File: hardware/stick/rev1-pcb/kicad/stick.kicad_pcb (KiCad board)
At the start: 4 copper layers, 60 x 30 mm, 13 parts, among them J1 USB4135-GF-A, J2 GDEY0154D67, SW1 BTN_L, SW2 BTN_R, U1 IP4292CZ12, U2 TPS2553, U3 AP2112K-3.3, U4 nRF52840, U5 ATECC608B, Y1 32MHz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

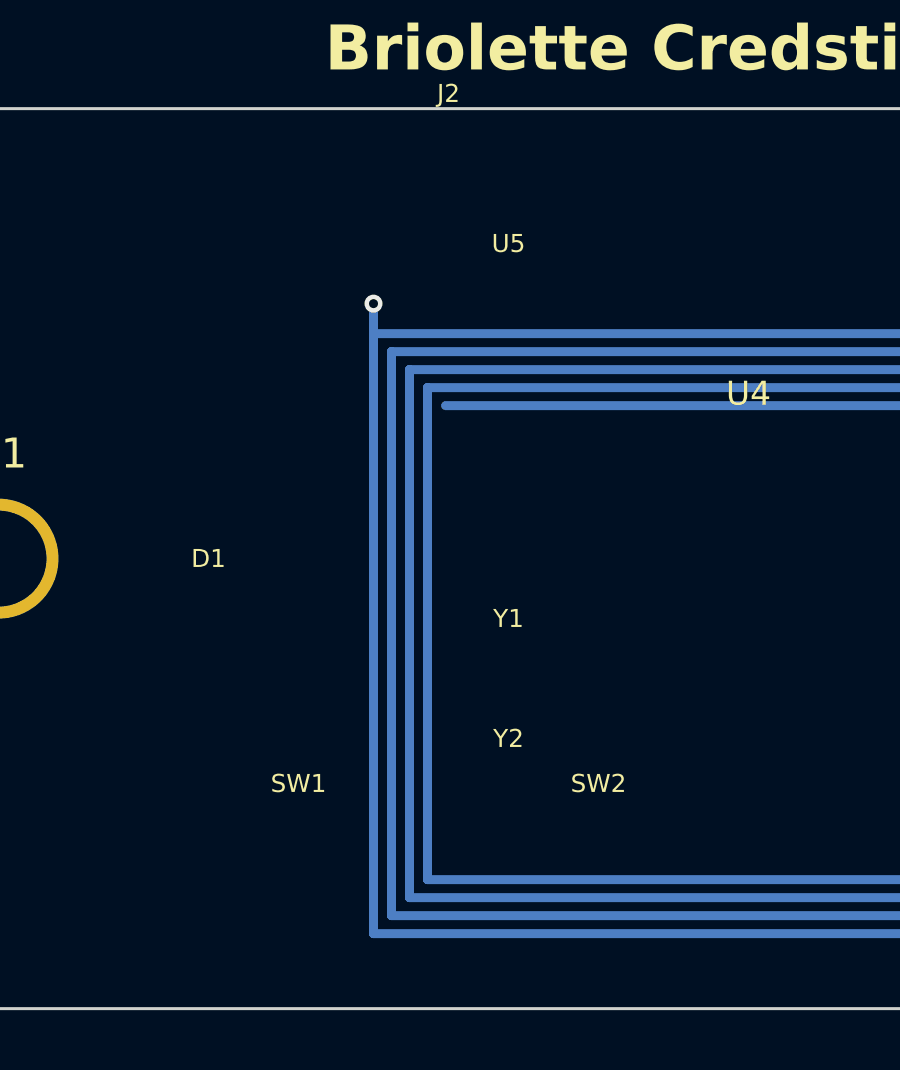
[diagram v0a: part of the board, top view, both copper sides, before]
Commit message: Fix DOA-causing issues in credstick and relay PCB designs
Critical fixes:
- HASL→ENIG copper finish on both PCBs (QFN pads need flat surface)
- Replace stale ATECC608B footprint with Nano-SIM connector on credstick PCB
- Fix NFC antenna spirals: closed rectangles→continuous spiral with crossover vias
- Fix TCA8418/SW3 component overlap at (-20,-15) on relay PCB
- Add missing inter-sheet pins (EPD_BUSY, BTN_L/R, LED, VSCAP_SENSE) to credstick top-level
- Fix button footprints (SW_SPST_PTS810→SW_SPST_3x3mm) to match schematic
- Replace stale I2C nets (SDA/SCL) with SIM interface nets
- Fix nRF52840 package description in both BOMs (aQFN-73 7x7→QFN-48 6x6)
- Remove ATECC608B reference from credstick BOM sourcing guide

https://claude.ai/code/session_01TM1rFxbipYtvAkh4Vt7My7
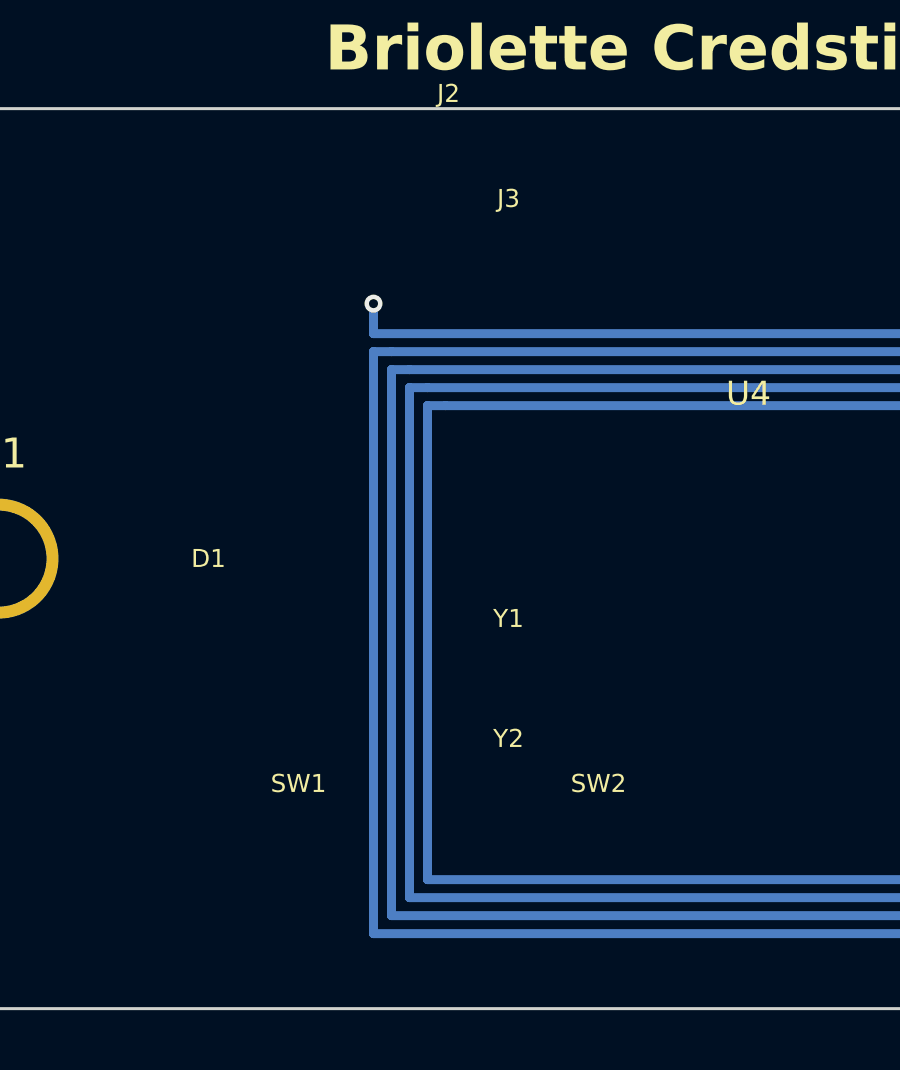
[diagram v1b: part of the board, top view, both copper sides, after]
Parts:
- removed U5: ATECC608B, stick-lib:UDFN-8-2x3mm
- added J3: Nano-SIM Push-Push, stick-lib:NanoSIM_Molex_78800, F.Cu at (-8.00, -8.00)
- SW1, SW2: footprint Button_Switch_SMD:SW_SPST_PTS810 -> stick-lib:SW_SPST_3x3mm
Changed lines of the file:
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@@
       (layer "B.Paste" (type "Bottom Solder Paste"))
       (layer "B.SilkS" (type "Bottom Silk Screen"))
-      (copper_finish "HASL with lead")
+      (copper_finish "ENIG")
       (dielectric_constraints no)
     )
@@
   (net 3 "VBUS")
   (net 4 "VSCAP")
-  (net 5 "SDA")
-  (net 6 "SCL")
+  (net 5 "SIM_IO")
+  (net 6 "SIM_CLK")
+  (net 29 "SIM_RST")
+  (net 30 "SIM_DET")
   (net 7 "SPI_SCK")
   (net 8 "SPI_MOSI")
@@
     )
   )
-  ;; --- ATECC608B: near MCU, I2C side ---
-  (footprint "stick-lib:UDFN-8-2x3mm"
+  ;; --- Nano-SIM connector: near MCU, ISO 7816 interface ---
+  (footprint "stick-lib:NanoSIM_Molex_78800"
     (layer "F.Cu")
     (at -8.0 -8.0 0)
-    (property "Reference" "U5"
-      (at 0 -2.5 0)
-      (layer "F.SilkS")
-      (effects (font (size 0.6 0.6) (thickness 0.1)))
-    )
-    (property "Value" "ATECC608B"
-      (at 0 2.5 0)
+    (property "Reference" "J3"
+      (at 0 -4.0 0)
+      (layer "F.SilkS")
+      (effects (font (size 0.6 0.6) (thickness 0.1)))
+    )
+    (property "Value" "Nano-SIM Push-Push"
+      (at 0 4.0 0)
       (layer "F.Fab")
       (effects (font (size 0.6 0.6) (thickness 0.1)))
@@
   )
   ;; --- Left button: below display, left side ---
-  (footprint "Button_Switch_SMD:SW_SPST_PTS810"
+  (footprint "stick-lib:SW_SPST_3x3mm"
     (layer "F.Cu")
     (at -15.0 10.0 0)
@@
   )
   ;; --- Right button: below display, right side ---
-  (footprint "Button_Switch_SMD:SW_SPST_PTS810"
+  (footprint "stick-lib:SW_SPST_3x3mm"
     (layer "F.Cu")
     (at -5.0 10.0 0)
@@
   ;; Centered at (0, 2) on the bottom layer
   ;; ============================================================
-  ;; Turn 1 (outermost): 25x20mm
-  (gr_line (start -12.5 -7.5) (end 12.5 -7.5)
-    (stroke (width 0.3) (type default)) (layer "B.Cu") (net 24))
-  (gr_line (start 12.5 -7.5) (end 12.5 12.5)
-    (stroke (width 0.3) (type default)) (layer "B.Cu") (net 24))
-  (gr_line (start 12.5 12.5) (end -12.5 12.5)
-    (stroke (width 0.3) (type default)) (layer "B.Cu") (net 24))
-  (gr_line (start -12.5 12.5) (end -12.5 -7.5)
-    (stroke (width 0.3) (type default)) (layer "B.Cu") (net 24))
-  ;; Turn 2: inset by 0.6mm (24.8x19.8 → ±11.9, ±6.9/±11.9)
-  (gr_line (start -11.9 -6.9) (end 11.9 -6.9)
-    (stroke (width 0.3) (type default)) (layer "B.Cu") (net 24))
-  (gr_line (start 11.9 -6.9) (end 11.9 11.9)
-    (stroke (width 0.3) (type default)) (layer "B.Cu") (net 24))
-  (gr_line (start 11.9 11.9) (end -11.9 11.9)
-    (stroke (width 0.3) (type default)) (layer "B.Cu") (net 24))
-  (gr_line (start -11.9 11.9) (end -11.9 -6.9)
-    (stroke (width 0.3) (type default)) (layer "B.Cu") (net 24))
-  ;; Turn 3: inset by another 0.6mm
-  (gr_line (start -11.3 -6.3) (end 11.3 -6.3)
-    (stroke (width 0.3) (type default)) (layer "B.Cu") (net 24))
-  (gr_line (start 11.3 -6.3) (end 11.3 11.3)
-    (stroke (width 0.3) (type default)) (layer "B.Cu") (net 24))
-  (gr_line (start 11.3 11.3) (end -11.3 11.3)
-    (stroke (width 0.3) (type default)) (layer "B.Cu") (net 24))
-  (gr_line (start -11.3 11.3) (end -11.3 -6.3)
-    (stroke (width 0.3) (type default)) (layer "B.Cu") (net 24))
-  ;; Turn 4: inset by another 0.6mm
-  (gr_line (start -10.7 -5.7) (end 10.7 -5.7)
-    (stroke (width 0.3) (type default)) (layer "B.Cu") (net 24))
-  (gr_line (start 10.7 -5.7) (end 10.7 10.7)
-    (stroke (width 0.3) (type default)) (layer "B.Cu") (net 24))
-  (gr_line (start 10.7 10.7) (end -10.7 10.7)
-    (stroke (width 0.3) (type default)) (layer "B.Cu") (net 24))
-  (gr_line (start -10.7 10.7) (end -10.7 -5.7)
-    (stroke (width 0.3) (type default)) (layer "B.Cu") (net 24))
-  ;; Turn 5 (innermost half-turn, connects to NFC2 via)
-  (gr_line (start -10.1 -5.1) (end 10.1 -5.1)
-    (stroke (width 0.3) (type default)) (layer "B.Cu") (net 25))
-  (gr_line (start 10.1 -5.1) (end 10.1 10.1)
-    (stroke (width 0.3) (type default)) (layer "B.Cu") (net 25))
-  ;; Spiral interconnects (short jumps between turns)
-  ;; Outer start → Turn 1 connects via trace to NFC1 pad via
-  (gr_line (start -12.5 -7.5) (end -12.5 -8.5)
-    (stroke (width 0.3) (type default)) (layer "B.Cu") (net 24))
-  ;; Inner end connects via to NFC2 pad
-  (gr_line (start 10.1 10.1) (end 10.1 11.0)
-    (stroke (width 0.3) (type default)) (layer "B.Cu") (net 25))
-  ;; NFC vias (connect bottom antenna to top-layer NFC pads)
+  ;; NFC Antenna: Continuous rectangular spiral, 4.5 turns
+  ;; Each turn is open at bottom-left corner and steps inward to next turn.
+  ;; Trace width: 0.3mm, spacing: 0.3mm, pitch: 0.6mm
+  ;; All turns on single net (NFC_ANT), inner end crosses to NFC2 via top layer.
+  ;; Start: via from F.Cu NFC1 pad down to B.Cu at (-12.5, -8.5)
   (via (at -12.5 -8.5) (size 0.6) (drill 0.3)
     (layers "F.Cu" "B.Cu") (net 24))
+  ;; Lead-in from via to Turn 1 start
+  (gr_line (start -12.5 -8.5) (end -12.5 -7.5)
+    (stroke (width 0.3) (type default)) (layer "B.Cu") (net 24))
+  ;; Turn 1 (outermost): 3 sides — top, right, bottom (open at left)
+  (gr_line (start -12.5 -7.5) (end 12.5 -7.5)
+    (stroke (width 0.3) (type default)) (layer "B.Cu") (net 24))
+  (gr_line (start 12.5 -7.5) (end 12.5 12.5)
+    (stroke (width 0.3) (type default)) (layer "B.Cu") (net 24))
+  (gr_line (start 12.5 12.5) (end -12.5 12.5)
+    (stroke (width 0.3) (type default)) (layer "B.Cu") (net 24))
+  ;; Left side stops short — step inward to Turn 2
+  (gr_line (start -12.5 12.5) (end -12.5 -6.9)
+    (stroke (width 0.3) (type default)) (layer "B.Cu") (net 24))
+  ;; Step inward (connects Turn 1 left to Turn 2 top-left)
+  (gr_line (start -12.5 -6.9) (end -11.9 -6.9)
+    (stroke (width 0.3) (type default)) (layer "B.Cu") (net 24))
+  ;; Turn 2: 3 sides — top, right, bottom (open at left)
+  (gr_line (start -11.9 -6.9) (end 11.9 -6.9)
+    (stroke (width 0.3) (type default)) (layer "B.Cu") (net 24))
+  (gr_line (start 11.9 -6.9) (end 11.9 11.9)
+    (stroke (width 0.3) (type default)) (layer "B.Cu") (net 24))
+  (gr_line (start 11.9 11.9) (end -11.9 11.9)
+    (stroke (width 0.3) (type default)) (layer "B.Cu") (net 24))
+  ;; Left side stops short — step inward to Turn 3
+  (gr_line (start -11.9 11.9) (end -11.9 -6.3)
+    (stroke (width 0.3) (type default)) (layer "B.Cu") (net 24))
+  (gr_line (start -11.9 -6.3) (end -11.3 -6.3)
+    (stroke (width 0.3) (type default)) (layer "B.Cu") (net 24))
+  ;; Turn 3: 3 sides — top, right, bottom (open at left)
+  (gr_line (start -11.3 -6.3) (end 11.3 -6.3)
+    (stroke (width 0.3) (type default)) (layer "B.Cu") (net 24))
+  (gr_line (start 11.3 -6.3) (end 11.3 11.3)
+    (stroke (width 0.3) (type default)) (layer "B.Cu") (net 24))
+  (gr_line (start 11.3 11.3) (end -11.3 11.3)
+    (stroke (width 0.3) (type default)) (layer "B.Cu") (net 24))
+  ;; Left side stops short — step inward to Turn 4
+  (gr_line (start -11.3 11.3) (end -11.3 -5.7)
+    (stroke (width 0.3) (type default)) (layer "B.Cu") (net 24))
+  (gr_line (start -11.3 -5.7) (end -10.7 -5.7)
+    (stroke (width 0.3) (type default)) (layer "B.Cu") (net 24))
+  ;; Turn 4: 3 sides — top, right, bottom (open at left)
+  (gr_line (start -10.7 -5.7) (end 10.7 -5.7)
+    (stroke (width 0.3) (type default)) (layer "B.Cu") (net 24))
+  (gr_line (start 10.7 -5.7) (end 10.7 10.7)
+    (stroke (width 0.3) (type default)) (layer "B.Cu") (net 24))
+  (gr_line (start 10.7 10.7) (end -10.7 10.7)
+    (stroke (width 0.3) (type default)) (layer "B.Cu") (net 24))
+  ;; Left side stops short — step inward to Turn 5
+  (gr_line (start -10.7 10.7) (end -10.7 -5.1)
+    (stroke (width 0.3) (type default)) (layer "B.Cu") (net 24))
+  (gr_line (start -10.7 -5.1) (end -10.1 -5.1)
+    (stroke (width 0.3) (type default)) (layer "B.Cu") (net 24))
+  ;; Turn 5 (innermost, half-turn): top and right side only
+  (gr_line (start -10.1 -5.1) (end 10.1 -5.1)
+    (stroke (width 0.3) (type default)) (layer "B.Cu") (net 24))
+  (gr_line (start 10.1 -5.1) (end 10.1 10.1)
+    (stroke (width 0.3) (type default)) (layer "B.Cu") (net 24))
+  ;; Lead-out from inner end to NFC2 via
+  (gr_line (start 10.1 10.1) (end 10.1 11.0)
+    (stroke (width 0.3) (type default)) (layer "B.Cu") (net 24))
+  ;; Crossover via: inner spiral end goes to F.Cu, then routes back to NFC2
+  ;; This via transitions the inner end to NFC2 net on the top layer
   (via (at 10.1 11.0) (size 0.6) (drill 0.3)
     (layers "F.Cu" "B.Cu") (net 25))

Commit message: Fix PCB files: convert invalid gr_line+net to segment elements
kicad-cli fails with "Failed to load board" (exit 3) because gr_line
doesn't support the (net N) property in KiCad's S-expression format.
NFC antenna traces on copper layers must use segment elements instead.

Also adds missing UUIDs to vias and zones (required by KiCad 8.0).

https://claude.ai/code/session_019dReYSafgEC1b8rTuLhQSc
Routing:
- net NFC_ANT1: track 0.00 -> 368.5 mm
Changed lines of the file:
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@@
     (layers "F.Cu" "B.Cu") (net 24))
   ;; Lead-in from via to Turn 1 start
-  (gr_line (start -12.5 -8.5) (end -12.5 -7.5)
-    (stroke (width 0.3) (type default)) (layer "B.Cu") (net 24))
+  (segment (start -12.5 -8.5) (end -12.5 -7.5) (width 0.3) (layer "B.Cu") (net 24))
   ;; Turn 1 (outermost): 3 sides — top, right, bottom (open at left)
-  (gr_line (start -12.5 -7.5) (end 12.5 -7.5)
-    (stroke (width 0.3) (type default)) (layer "B.Cu") (net 24))
-  (gr_line (start 12.5 -7.5) (end 12.5 12.5)
-    (stroke (width 0.3) (type default)) (layer "B.Cu") (net 24))
-  (gr_line (start 12.5 12.5) (end -12.5 12.5)
-    (stroke (width 0.3) (type default)) (layer "B.Cu") (net 24))
+  (segment (start -12.5 -7.5) (end 12.5 -7.5) (width 0.3) (layer "B.Cu") (net 24))
+  (segment (start 12.5 -7.5) (end 12.5 12.5) (width 0.3) (layer "B.Cu") (net 24))
+  (segment (start 12.5 12.5) (end -12.5 12.5) (width 0.3) (layer "B.Cu") (net 24))
   ;; Left side stops short — step inward to Turn 2
-  (gr_line (start -12.5 12.5) (end -12.5 -6.9)
-    (stroke (width 0.3) (type default)) (layer "B.Cu") (net 24))
+  (segment (start -12.5 12.5) (end -12.5 -6.9) (width 0.3) (layer "B.Cu") (net 24))
   ;; Step inward (connects Turn 1 left to Turn 2 top-left)
-  (gr_line (start -12.5 -6.9) (end -11.9 -6.9)
-    (stroke (width 0.3) (type default)) (layer "B.Cu") (net 24))
+  (segment (start -12.5 -6.9) (end -11.9 -6.9) (width 0.3) (layer "B.Cu") (net 24))
   ;; Turn 2: 3 sides — top, right, bottom (open at left)
-  (gr_line (start -11.9 -6.9) (end 11.9 -6.9)
-    (stroke (width 0.3) (type default)) (layer "B.Cu") (net 24))
-  (gr_line (start 11.9 -6.9) (end 11.9 11.9)
-    (stroke (width 0.3) (type default)) (layer "B.Cu") (net 24))
-  (gr_line (start 11.9 11.9) (end -11.9 11.9)
-    (stroke (width 0.3) (type default)) (layer "B.Cu") (net 24))
+  (segment (start -11.9 -6.9) (end 11.9 -6.9) (width 0.3) (layer "B.Cu") (net 24))
+  (segment (start 11.9 -6.9) (end 11.9 11.9) (width 0.3) (layer "B.Cu") (net 24))
+  (segment (start 11.9 11.9) (end -11.9 11.9) (width 0.3) (layer "B.Cu") (net 24))
   ;; Left side stops short — step inward to Turn 3
-  (gr_line (start -11.9 11.9) (end -11.9 -6.3)
-    (stroke (width 0.3) (type default)) (layer "B.Cu") (net 24))
-  (gr_line (start -11.9 -6.3) (end -11.3 -6.3)
-    (stroke (width 0.3) (type default)) (layer "B.Cu") (net 24))
+  (segment (start -11.9 11.9) (end -11.9 -6.3) (width 0.3) (layer "B.Cu") (net 24))
+  (segment (start -11.9 -6.3) (end -11.3 -6.3) (width 0.3) (layer "B.Cu") (net 24))
   ;; Turn 3: 3 sides — top, right, bottom (open at left)
-  (gr_line (start -11.3 -6.3) (end 11.3 -6.3)
-    (stroke (width 0.3) (type default)) (layer "B.Cu") (net 24))
-  (gr_line (start 11.3 -6.3) (end 11.3 11.3)
-    (stroke (width 0.3) (type default)) (layer "B.Cu") (net 24))
-  (gr_line (start 11.3 11.3) (end -11.3 11.3)
-    (stroke (width 0.3) (type default)) (layer "B.Cu") (net 24))
+  (segment (start -11.3 -6.3) (end 11.3 -6.3) (width 0.3) (layer "B.Cu") (net 24))
+  (segment (start 11.3 -6.3) (end 11.3 11.3) (width 0.3) (layer "B.Cu") (net 24))
+  (segment (start 11.3 11.3) (end -11.3 11.3) (width 0.3) (layer "B.Cu") (net 24))
   ;; Left side stops short — step inward to Turn 4
-  (gr_line (start -11.3 11.3) (end -11.3 -5.7)
-    (stroke (width 0.3) (type default)) (layer "B.Cu") (net 24))
-  (gr_line (start -11.3 -5.7) (end -10.7 -5.7)
-    (stroke (width 0.3) (type default)) (layer "B.Cu") (net 24))
+  (segment (start -11.3 11.3) (end -11.3 -5.7) (width 0.3) (layer "B.Cu") (net 24))
+  (segment (start -11.3 -5.7) (end -10.7 -5.7) (width 0.3) (layer "B.Cu") (net 24))
   ;; Turn 4: 3 sides — top, right, bottom (open at left)
-  (gr_line (start -10.7 -5.7) (end 10.7 -5.7)
-    (stroke (width 0.3) (type default)) (layer "B.Cu") (net 24))
-  (gr_line (start 10.7 -5.7) (end 10.7 10.7)
-    (stroke (width 0.3) (type default)) (layer "B.Cu") (net 24))
-  (gr_line (start 10.7 10.7) (end -10.7 10.7)
-    (stroke (width 0.3) (type default)) (layer "B.Cu") (net 24))
+  (segment (start -10.7 -5.7) (end 10.7 -5.7) (width 0.3) (layer "B.Cu") (net 24))
+  (segment (start 10.7 -5.7) (end 10.7 10.7) (width 0.3) (layer "B.Cu") (net 24))
+  (segment (start 10.7 10.7) (end -10.7 10.7) (width 0.3) (layer "B.Cu") (net 24))
   ;; Left side stops short — step inward to Turn 5
-  (gr_line (start -10.7 10.7) (end -10.7 -5.1)
-    (stroke (width 0.3) (type default)) (layer "B.Cu") (net 24))
-  (gr_line (start -10.7 -5.1) (end -10.1 -5.1)
-    (stroke (width 0.3) (type default)) (layer "B.Cu") (net 24))
+  (segment (start -10.7 10.7) (end -10.7 -5.1) (width 0.3) (layer "B.Cu") (net 24))
+  (segment (start -10.7 -5.1) (end -10.1 -5.1) (width 0.3) (layer "B.Cu") (net 24))
   ;; Turn 5 (innermost, half-turn): top and right side only
-  (gr_line (start -10.1 -5.1) (end 10.1 -5.1)
-    (stroke (width 0.3) (type default)) (layer "B.Cu") (net 24))
-  (gr_line (start 10.1 -5.1) (end 10.1 10.1)
-    (stroke (width 0.3) (type default)) (layer "B.Cu") (net 24))
+  (segment (start -10.1 -5.1) (end 10.1 -5.1) (width 0.3) (layer "B.Cu") (net 24))
+  (segment (start 10.1 -5.1) (end 10.1 10.1) (width 0.3) (layer "B.Cu") (net 24))
   ;; Lead-out from inner end to NFC2 via
-  (gr_line (start 10.1 10.1) (end 10.1 11.0)
-    (stroke (width 0.3) (type default)) (layer "B.Cu") (net 24))
+  (segment (start 10.1 10.1) (end 10.1 11.0) (width 0.3) (layer "B.Cu") (net 24))
   ;; Crossover via: inner spiral end goes to F.Cu, then routes back to NFC2
   ;; This via transitions the inner end to NFC2 net on the top layer
@@
     (net_name "GND")
     (layer "In1.Cu")
-    (uuid "zone-gnd-in1")
     (hatch edge 0.5)
     (connect_pads (clearance 0.3))
@@
     (net_name "VCC")
     (layer "In2.Cu")
-    (uuid "zone-vcc-in2")
     (hatch edge 0.5)
     (connect_pads (clearance 0.3))
@@
     (net_name "GND")
     (layer "B.Cu")
-    (uuid "zone-gnd-bcu")
     (hatch edge 0.5)
     (connect_pads (clearance 0.3))
@@
     (net_name "")
     (layer "In1.Cu")
-    (uuid "zone-keepout-nfc-gnd")
     (hatch edge 0.5)
     (connect_pads (clearance 0))
@@
     (net_name "")
     (layer "In2.Cu")
-    (uuid "zone-keepout-nfc-pwr")
     (hatch edge 0.5)
     (connect_pads (clearance 0))
